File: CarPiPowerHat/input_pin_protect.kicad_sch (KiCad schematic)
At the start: 7 parts

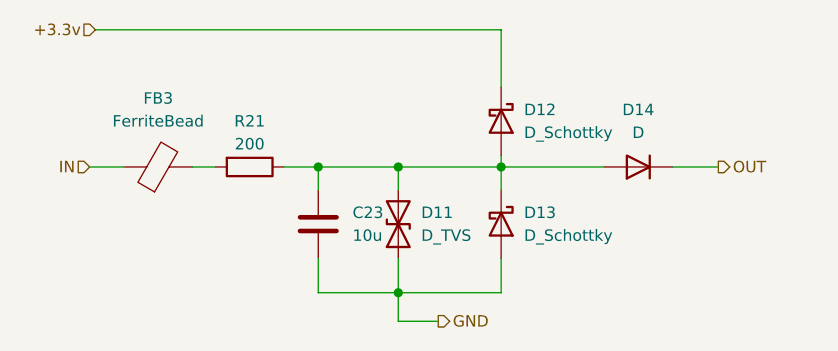
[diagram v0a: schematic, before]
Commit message: updated layout
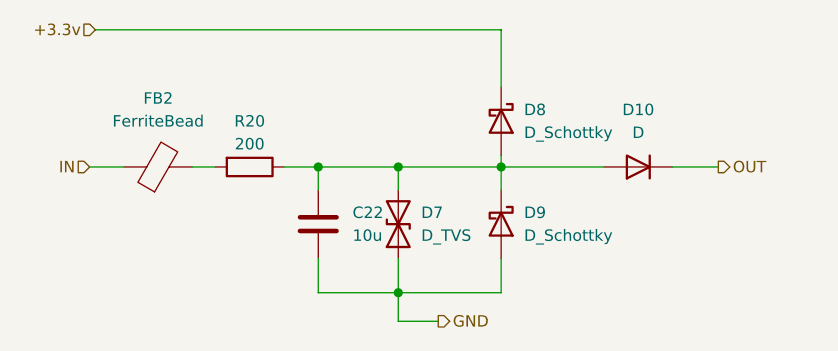
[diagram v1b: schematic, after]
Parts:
- renumbered C23 to C22, D14 to D10, D11 to D7, D12 to D8, D13 to D9, FB3 to FB2, R21 to R20
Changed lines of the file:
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@@
-(kicad_sch (version 20210126) (generator eeschema)
+(kicad_sch (version 20210406) (generator eeschema)
   (paper "A4")
   (junction (at 129.54 80.01) (diameter 1.016) (color 0 0 0 0))
@@
   (symbol (lib_id "Device:R") (at 121.92 80.01 270)
     (in_bom yes) (on_board yes)
-    (property "Reference" "R21" (id 0) (at 121.92 74.93 90))
+    (property "Reference" "R20" (id 0) (at 121.92 74.93 90))
     (property "Value" "200" (id 1) (at 121.92 77.47 90))
     (property "Footprint" "Resistor_SMD:R_0402_1005Metric" (id 2) (at 121.92 78.232 90)
@@
   (symbol (lib_id "Device:D_TVS") (at 138.43 86.36 90)
     (in_bom yes) (on_board yes)
-    (property "Reference" "D11" (id 0) (at 140.97 85.09 90)
+    (property "Reference" "D7" (id 0) (at 140.97 85.09 90)
       (effects (font (size 1.27 1.27)) (justify right))
     )
@@
   (symbol (lib_id "Device:D_Schottky") (at 149.86 74.93 270)
     (in_bom yes) (on_board yes)
-    (property "Reference" "D12" (id 0) (at 152.4 73.66 90)
+    (property "Reference" "D8" (id 0) (at 152.4 73.66 90)
       (effects (font (size 1.27 1.27)) (justify left))
     )
@@
   (symbol (lib_id "Device:D_Schottky") (at 149.86 86.36 270)
     (in_bom yes) (on_board yes)
-    (property "Reference" "D13" (id 0) (at 152.4 85.09 90)
+    (property "Reference" "D9" (id 0) (at 152.4 85.09 90)
       (effects (font (size 1.27 1.27)) (justify left))
     )
@@
   (symbol (lib_id "Device:D") (at 165.1 80.01 180)
     (in_bom yes) (on_board yes)
-    (property "Reference" "D14" (id 0) (at 165.1 73.66 0))
+    (property "Reference" "D10" (id 0) (at 165.1 73.66 0))
     (property "Value" "D" (id 1) (at 165.1 76.2 0))
     (property "Footprint" "Diode_SMD:D_SOD-123F" (id 2) (at 165.1 80.01 0)
@@
   (symbol (lib_id "Device:C") (at 129.54 86.36 0)
     (in_bom yes) (on_board yes)
-    (property "Reference" "C23" (id 0) (at 133.35 85.09 0)
+    (property "Reference" "C22" (id 0) (at 133.35 85.09 0)
       (effects (font (size 1.27 1.27)) (justify left))
     )
@@
   (symbol (lib_id "Device:FerriteBead") (at 111.76 80.01 90)
     (in_bom yes) (on_board yes)
-    (property "Reference" "FB3" (id 0) (at 111.76 72.39 90))
+    (property "Reference" "FB2" (id 0) (at 111.76 72.39 90))
     (property "Value" "FerriteBead" (id 1) (at 111.76 74.93 90))
     (property "Footprint" "Resistor_SMD:R_0805_2012Metric" (id 2) (at 111.76 81.788 90)

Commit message: Finished Layout
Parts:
- removed D10: D, Diode_SMD:D_SOD-123F, symbol Device:D
- removed D9: D_Schottky, Diode_SMD:D_SOD-123, symbol Device:D_Schottky
- removed FB2: FerriteBead, Resistor_SMD:R_0805_2012Metric, symbol Device:FerriteBead
- added D5: BAT54S, Package_TO_SOT_SMD:SOT-23, symbol Diode:BAT54S
- C22: value 10u -> 10uF; footprint Resistor_SMD:R_0603_1608Metric -> Capacitor_SMD:C_0603_1608Metric
- D7: value D_TVS -> TPGBLC12C; footprint Diode_SMD:D_0603_1608Metric -> Diode_SMD:D_SOD-323; LCSC (none) -> C587149
- D8: value D_Schottky -> D_Schottky 15mA; footprint Diode_SMD:D_SOD-123 -> Diode_SMD:D_SOD-323; LCSC C8598 -> C508253
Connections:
- net +3.3v: now also D5.2; no longer D8.1 (K)
- net GND: now also D5.1
- net IN: now also R20.2
- net OUT: now also D8.1 (K)
- net at C22.1, D7.2 (A2), R20.1: no longer D8.2 (A)
- new net: D5.3, D8.2 (A)
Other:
- moved on the sheet: D7
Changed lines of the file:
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@@
   (paper "A4")
   (junction (at 129.54 80.01) (diameter 1.016) (color 0 0 0 0))
-  (junction (at 138.43 80.01) (diameter 1.016) (color 0 0 0 0))
-  (junction (at 138.43 93.98) (diameter 1.016) (color 0 0 0 0))
-  (junction (at 149.86 80.01) (diameter 1.016) (color 0 0 0 0))
-  (wire (pts (xy 104.14 80.01) (xy 107.95 80.01))
+  (junction (at 143.51 80.01) (diameter 1.016) (color 0 0 0 0))
+  (junction (at 143.51 93.98) (diameter 1.016) (color 0 0 0 0))
+  (wire (pts (xy 104.14 80.01) (xy 118.11 80.01))
     (stroke (width 0) (type solid) (color 0 0 0 0))
   )
-  (wire (pts (xy 104.775 64.77) (xy 149.86 64.77))
-    (stroke (width 0) (type solid) (color 0 0 0 0))
-  )
-  (wire (pts (xy 115.57 80.01) (xy 118.11 80.01))
+  (wire (pts (xy 104.775 64.77) (xy 154.94 64.77))
     (stroke (width 0) (type solid) (color 0 0 0 0))
   )
@@
     (stroke (width 0) (type solid) (color 0 0 0 0))
   )
-  (wire (pts (xy 129.54 80.01) (xy 138.43 80.01))
+  (wire (pts (xy 129.54 80.01) (xy 143.51 80.01))
     (stroke (width 0) (type solid) (color 0 0 0 0))
   )
@@
     (stroke (width 0) (type solid) (color 0 0 0 0))
   )
-  (wire (pts (xy 129.54 93.98) (xy 138.43 93.98))
+  (wire (pts (xy 129.54 93.98) (xy 143.51 93.98))
     (stroke (width 0) (type solid) (color 0 0 0 0))
   )
-  (wire (pts (xy 138.43 80.01) (xy 149.86 80.01))
+  (wire (pts (xy 143.51 80.01) (xy 154.94 80.01))
     (stroke (width 0) (type solid) (color 0 0 0 0))
   )
-  (wire (pts (xy 138.43 82.55) (xy 138.43 80.01))
+  (wire (pts (xy 143.51 82.55) (xy 143.51 80.01))
     (stroke (width 0) (type solid) (color 0 0 0 0))
   )
-  (wire (pts (xy 138.43 93.98) (xy 138.43 90.17))
+  (wire (pts (xy 143.51 93.98) (xy 143.51 90.17))
     (stroke (width 0) (type solid) (color 0 0 0 0))
   )
-  (wire (pts (xy 138.43 93.98) (xy 138.43 97.155))
+  (wire (pts (xy 143.51 93.98) (xy 143.51 97.155))
     (stroke (width 0) (type solid) (color 0 0 0 0))
   )
-  (wire (pts (xy 138.43 97.155) (xy 142.875 97.155))
+  (wire (pts (xy 143.51 97.155) (xy 147.955 97.155))
     (stroke (width 0) (type solid) (color 0 0 0 0))
   )
-  (wire (pts (xy 149.86 64.77) (xy 149.86 71.12))
+  (wire (pts (xy 154.94 64.77) (xy 154.94 72.39))
     (stroke (width 0) (type solid) (color 0 0 0 0))
   )
-  (wire (pts (xy 149.86 78.74) (xy 149.86 80.01))
+  (wire (pts (xy 154.94 87.63) (xy 154.94 93.98))
     (stroke (width 0) (type solid) (color 0 0 0 0))
   )
-  (wire (pts (xy 149.86 80.01) (xy 149.86 82.55))
+  (wire (pts (xy 154.94 93.98) (xy 143.51 93.98))
     (stroke (width 0) (type solid) (color 0 0 0 0))
   )
-  (wire (pts (xy 149.86 80.01) (xy 161.29 80.01))
+  (wire (pts (xy 160.02 80.01) (xy 166.37 80.01))
     (stroke (width 0) (type solid) (color 0 0 0 0))
   )
-  (wire (pts (xy 149.86 90.17) (xy 149.86 93.98))
-    (stroke (width 0) (type solid) (color 0 0 0 0))
-  )
-  (wire (pts (xy 149.86 93.98) (xy 138.43 93.98))
-    (stroke (width 0) (type solid) (color 0 0 0 0))
-  )
-  (wire (pts (xy 168.91 80.01) (xy 173.99 80.01))
+  (wire (pts (xy 173.99 80.01) (xy 179.07 80.01))
     (stroke (width 0) (type solid) (color 0 0 0 0))
   )
@@
     (effects (font (size 1.27 1.27)) (justify right))
   )
-  (hierarchical_label "GND" (shape output) (at 142.875 97.155 0)
+  (hierarchical_label "GND" (shape output) (at 147.955 97.155 0)
     (effects (font (size 1.27 1.27)) (justify left))
   )
-  (hierarchical_label "OUT" (shape output) (at 173.99 80.01 0)
+  (hierarchical_label "OUT" (shape output) (at 179.07 80.01 0)
     (effects (font (size 1.27 1.27)) (justify left))
   )
@@
     (pin "2")
   )
-  (symbol (lib_id "Device:D_TVS") (at 138.43 86.36 90)
+  (symbol (lib_id "Device:D_TVS") (at 143.51 86.36 90)
     (in_bom yes) (on_board yes)
-    (property "Reference" "D7" (id 0) (at 140.97 85.09 90)
+    (property "Reference" "D7" (id 0) (at 146.05 85.09 90)
       (effects (font (size 1.27 1.27)) (justify right))
     )
-    (property "Value" "D_TVS" (id 1) (at 140.97 87.63 90)
+    (property "Value" "TPGBLC12C" (id 1) (at 146.05 87.63 90)
       (effects (font (size 1.27 1.27)) (justify right))
     )
-    (property "Footprint" "Diode_SMD:D_0603_1608Metric" (id 2) (at 138.43 86.36 0)
+    (property "Footprint" "Diode_SMD:D_SOD-323" (id 2) (at 143.51 86.36 0)
       (effects (font (size 1.27 1.27)) hide)
     )
-    (property "Datasheet" "~" (id 3) (at 138.43 86.36 0)
+    (property "Datasheet" "~" (id 3) (at 143.51 86.36 0)
+      (effects (font (size 1.27 1.27)) hide)
+    )
+    (property "LCSC" "C587149" (id 4) (at 143.51 86.36 90)
       (effects (font (size 1.27 1.27)) hide)
     )
@@
     (pin "2")
   )
-  (symbol (lib_id "Device:D_Schottky") (at 149.86 74.93 270)
-    (in_bom yes) (on_board yes)
-    (property "Reference" "D8" (id 0) (at 152.4 73.66 90)
-      (effects (font (size 1.27 1.27)) (justify left))
-    )
-    (property "Value" "D_Schottky" (id 1) (at 152.4 76.2 90)
-      (effects (font (size 1.27 1.27)) (justify left))
-    )
-    (property "Footprint" "Diode_SMD:D_SOD-123" (id 2) (at 149.86 74.93 0)
+  (symbol (lib_id "Device:D_Schottky") (at 170.18 80.01 180)
+    (in_bom yes) (on_board yes) (fields_autoplaced)
+    (property "Reference" "D8" (id 0) (at 170.18 73.66 0))
+    (property "Value" "D_Schottky 15mA" (id 1) (at 170.18 76.2 0))
+    (property "Footprint" "Diode_SMD:D_SOD-323" (id 2) (at 170.18 80.01 0)
       (effects (font (size 1.27 1.27)) hide)
     )
-    (property "Datasheet" "~" (id 3) (at 149.86 74.93 0)
+    (property "Datasheet" "~" (id 3) (at 170.18 80.01 0)
       (effects (font (size 1.27 1.27)) hide)
     )
-    (property "LCSC" "C8598" (id 4) (at 149.86 74.93 90)
-      (effects (font (size 1.27 1.27)) hide)
-    )
-    (pin "1")
-    (pin "2")
-  )
-  (symbol (lib_id "Device:D_Schottky") (at 149.86 86.36 270)
-    (in_bom yes) (on_board yes)
-    (property "Reference" "D9" (id 0) (at 152.4 85.09 90)
-      (effects (font (size 1.27 1.27)) (justify left))
-    )
-    (property "Value" "D_Schottky" (id 1) (at 152.4 87.63 90)
-      (effects (font (size 1.27 1.27)) (justify left))
-    )
-    (property "Footprint" "Diode_SMD:D_SOD-123" (id 2) (at 149.86 86.36 0)
-      (effects (font (size 1.27 1.27)) hide)
-    )
-    (property "Datasheet" "~" (id 3) (at 149.86 86.36 0)
-      (effects (font (size 1.27 1.27)) hide)
-    )
-    (pin "1")
-    (pin "2")
-  )
-  (symbol (lib_id "Device:D") (at 165.1 80.01 180)
-    (in_bom yes) (on_board yes)
-    (property "Reference" "D10" (id 0) (at 165.1 73.66 0))
-    (property "Value" "D" (id 1) (at 165.1 76.2 0))
-    (property "Footprint" "Diode_SMD:D_SOD-123F" (id 2) (at 165.1 80.01 0)
-      (effects (font (size 1.27 1.27)) hide)
-    )
-    (property "Datasheet" "~" (id 3) (at 165.1 80.01 0)
-      (effects (font (size 1.27 1.27)) hide)
-    )
-    (property "LCSC" "C64898" (id 4) (at 165.1 80.01 0)
+    (property "LCSC" "C508253" (id 4) (at 170.18 80.01 0)
       (effects (font (size 1.27 1.27)) hide)
     )
@@
   (symbol (lib_id "Device:C") (at 129.54 86.36 0)
     (in_bom yes) (on_board yes)
-    (property "Reference" "C22" (id 0) (at 133.35 85.09 0)
+    (property "Reference" "C22" (id 0) (at 133.985 85.09 0)
       (effects (font (size 1.27 1.27)) (justify left))
     )
-    (property "Value" "10u" (id 1) (at 133.35 87.63 0)
+    (property "Value" "10uF" (id 1) (at 133.985 87.63 0)
       (effects (font (size 1.27 1.27)) (justify left))
     )
-    (property "Footprint" "Resistor_SMD:R_0603_1608Metric" (id 2) (at 130.5052 90.17 0)
+    (property "Footprint" "Capacitor_SMD:C_0603_1608Metric" (id 2) (at 130.5052 90.17 0)
       (effects (font (size 1.27 1.27)) hide)
     )
@@
     (pin "2")
   )
-  (symbol (lib_id "Device:FerriteBead") (at 111.76 80.01 90)
+  (symbol (lib_id "Diode:BAT54S") (at 154.94 80.01 90)
     (in_bom yes) (on_board yes)
-    (property "Reference" "FB2" (id 0) (at 111.76 72.39 90))
-    (property "Value" "FerriteBead" (id 1) (at 111.76 74.93 90))
-    (property "Footprint" "Resistor_SMD:R_0805_2012Metric" (id 2) (at 111.76 81.788 90)
-      (effects (font (size 1.27 1.27)) hide)
+    (property "Reference" "D5" (id 0) (at 163.83 78.7399 90)
+      (effects (font (size 1.27 1.27)) (justify left))
     )
-    (property "Datasheet" "~" (id 3) (at 111.76 80.01 0)
+    (property "Value" "BAT54S" (id 1) (at 163.83 81.2799 90)
+      (effects (font (size 1.27 1.27)) (justify left))
+    )
+    (property "Footprint" "Package_TO_SOT_SMD:SOT-23" (id 2) (at 151.765 78.105 0)
+      (effects (font (size 1.27 1.27)) (justify left) hide)
+    )
+    (property "Datasheet" "https://www.diodes.com/assets/Datasheets/ds11005.pdf" (id 3) (at 154.94 83.058 0)
       (effects (font (size 1.27 1.27)) hide)
     )
     (pin "1")
     (pin "2")
+    (pin "3")
   )
 )

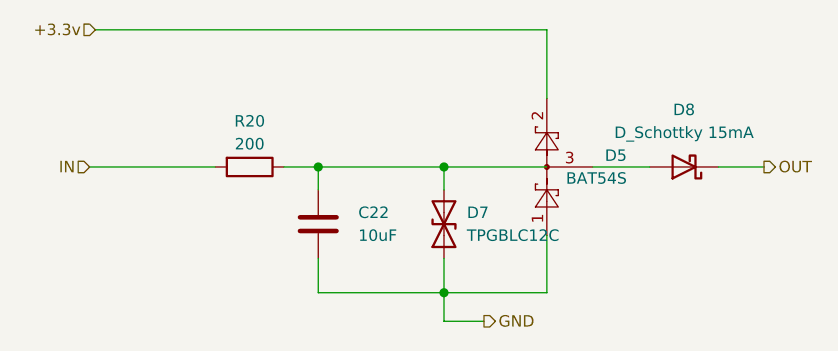
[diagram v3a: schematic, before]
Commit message: Added part numbers
* Selected parts from lcsc
* Checked footprints
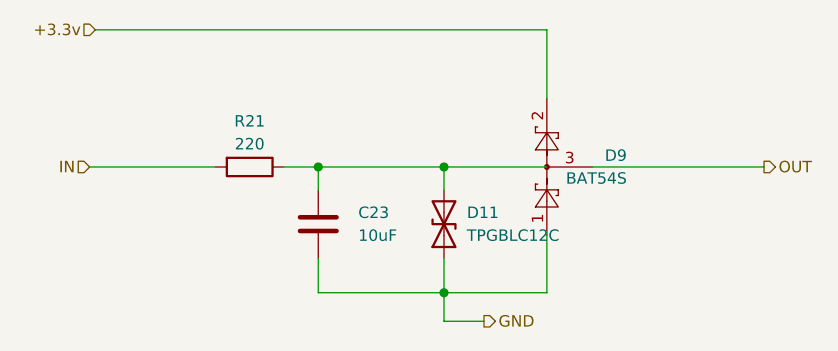
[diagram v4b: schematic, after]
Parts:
- removed D8: D_Schottky 15mA, Diode_SMD:D_SOD-323, symbol Device:D_Schottky
- C23: renamed from C22; footprint Capacitor_SMD:C_0603_1608Metric -> Capacitor_SMD:C_0805_2012Metric; Field4 (none) -> Digikey; Field6 (none) -> GRM21BR71A106KA73L; LCSC (none) -> C15850
- D9: renamed from D5; LCSC (none) -> C408389
- R21: renamed from R20; value 200 -> 220; LCSC (none) -> C25091
- renumbered D7 to D11
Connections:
- net OUT: now also D9.3
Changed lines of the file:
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@@
     (stroke (width 0) (type solid) (color 0 0 0 0))
   )
-  (wire (pts (xy 160.02 80.01) (xy 166.37 80.01))
-    (stroke (width 0) (type solid) (color 0 0 0 0))
-  )
-  (wire (pts (xy 173.99 80.01) (xy 179.07 80.01))
+  (wire (pts (xy 160.02 80.01) (xy 179.07 80.01))
     (stroke (width 0) (type solid) (color 0 0 0 0))
   )
@@
   (symbol (lib_id "Device:R") (at 121.92 80.01 270)
     (in_bom yes) (on_board yes)
-    (property "Reference" "R20" (id 0) (at 121.92 74.93 90))
-    (property "Value" "200" (id 1) (at 121.92 77.47 90))
+    (property "Reference" "R21" (id 0) (at 121.92 74.93 90))
+    (property "Value" "220" (id 1) (at 121.92 77.47 90))
     (property "Footprint" "Resistor_SMD:R_0402_1005Metric" (id 2) (at 121.92 78.232 90)
       (effects (font (size 1.27 1.27)) hide)
     )
     (property "Datasheet" "~" (id 3) (at 121.92 80.01 0)
+      (effects (font (size 1.27 1.27)) hide)
+    )
+    (property "LCSC" "C25091" (id 4) (at 121.92 80.01 0)
       (effects (font (size 1.27 1.27)) hide)
     )
@@
   (symbol (lib_id "Device:D_TVS") (at 143.51 86.36 90)
     (in_bom yes) (on_board yes)
-    (property "Reference" "D7" (id 0) (at 146.05 85.09 90)
+    (property "Reference" "D11" (id 0) (at 146.05 85.09 90)
       (effects (font (size 1.27 1.27)) (justify right))
     )
@@
     (pin "2")
   )
-  (symbol (lib_id "Device:D_Schottky") (at 170.18 80.01 180)
-    (in_bom yes) (on_board yes) (fields_autoplaced)
-    (property "Reference" "D8" (id 0) (at 170.18 73.66 0))
-    (property "Value" "D_Schottky 15mA" (id 1) (at 170.18 76.2 0))
-    (property "Footprint" "Diode_SMD:D_SOD-323" (id 2) (at 170.18 80.01 0)
-      (effects (font (size 1.27 1.27)) hide)
-    )
-    (property "Datasheet" "~" (id 3) (at 170.18 80.01 0)
-      (effects (font (size 1.27 1.27)) hide)
-    )
-    (property "LCSC" "C508253" (id 4) (at 170.18 80.01 0)
-      (effects (font (size 1.27 1.27)) hide)
-    )
-    (pin "1")
-    (pin "2")
-  )
   (symbol (lib_id "Device:C") (at 129.54 86.36 0)
     (in_bom yes) (on_board yes)
-    (property "Reference" "C22" (id 0) (at 133.985 85.09 0)
+    (property "Reference" "C23" (id 0) (at 133.985 85.09 0)
       (effects (font (size 1.27 1.27)) (justify left))
     )
@@
       (effects (font (size 1.27 1.27)) (justify left))
     )
-    (property "Footprint" "Capacitor_SMD:C_0603_1608Metric" (id 2) (at 130.5052 90.17 0)
+    (property "Footprint" "Capacitor_SMD:C_0805_2012Metric" (id 2) (at 130.5052 90.17 0)
       (effects (font (size 1.27 1.27)) hide)
     )
     (property "Datasheet" "~" (id 3) (at 129.54 86.36 0)
+      (effects (font (size 1.27 1.27)) hide)
+    )
+    (property "Field4" "Digikey" (id 4) (at 129.54 86.36 0)
+      (effects (font (size 1.27 1.27)) hide)
+    )
+    (property "Field6" "GRM21BR71A106KA73L" (id 5) (at 129.54 86.36 0)
+      (effects (font (size 1.27 1.27)) hide)
+    )
+    (property "LCSC" "C15850" (id 6) (at 129.54 86.36 0)
       (effects (font (size 1.27 1.27)) hide)
     )
@@
   (symbol (lib_id "Diode:BAT54S") (at 154.94 80.01 90)
     (in_bom yes) (on_board yes)
-    (property "Reference" "D5" (id 0) (at 163.83 78.7399 90)
+    (property "Reference" "D9" (id 0) (at 163.83 78.7399 90)
       (effects (font (size 1.27 1.27)) (justify left))
     )
@@
       (effects (font (size 1.27 1.27)) hide)
     )
+    (property "LCSC" "C408389" (id 4) (at 154.94 80.01 0)
+      (effects (font (size 1.27 1.27)) hide)
+    )
